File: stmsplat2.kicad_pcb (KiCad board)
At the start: 2 copper layers, 97 parts, among them J1 C11_2X36, J10 Conn_01x03_Male, J11 Conn_01x02_Male, J12 Conn_01x04_Male, J13 Conn_01x04_Male, J14 Conn_01x02, J15 Conn_01x02, J16 Screw_Terminal_01x03, J17 Screw_Terminal_01x02, J2 C12_2X36, J3 Conn_01x04_Male, J4 Conn_01x04_Male, J5 Conn_Coaxial, J6 Conn_01x06, J7 Conn_01x04_Male, J8 Conn_01x04_Male, J9 Conn_01x03_Male, Q1 BSS138LT1G, U1 ublox_chinese_PCB_module, U10 XCVR_E30-400M20S, U2 ESP32-C3-13, U3 SST25VF032B, U4 48L512-48LM01, U5 Opamp_Quad_MCP6024, U6 E180-ZG120A, U7 AZ1084C, U8 MCP6S93-X_UN, U9 DS2485

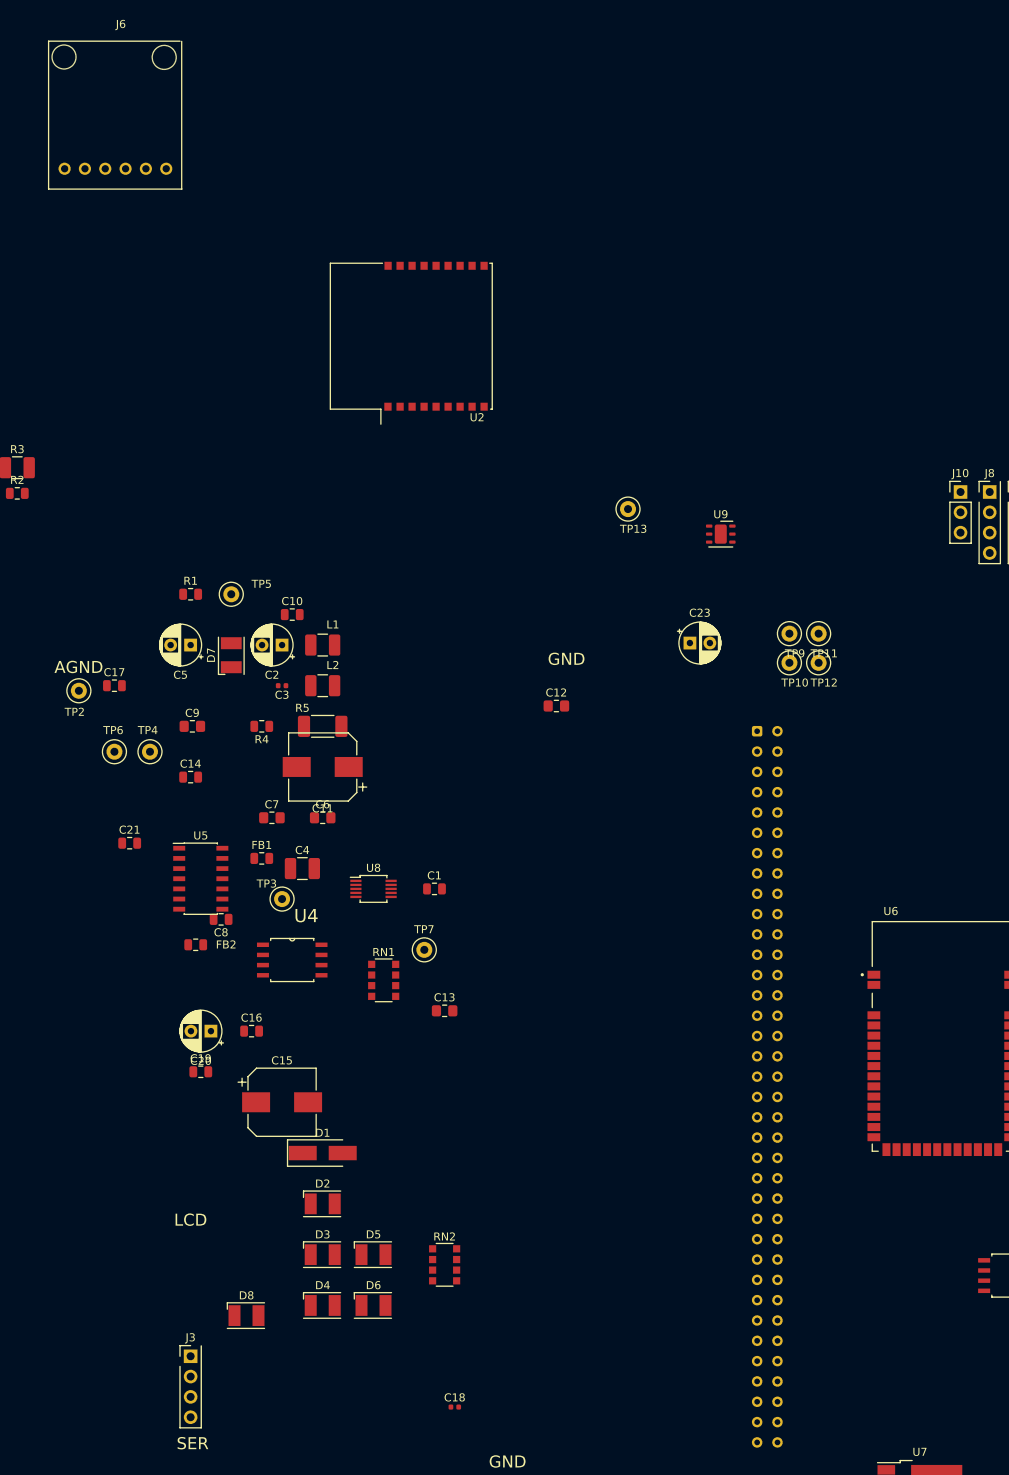
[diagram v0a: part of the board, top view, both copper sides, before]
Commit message: updated 3115 module footprint and on the PCB
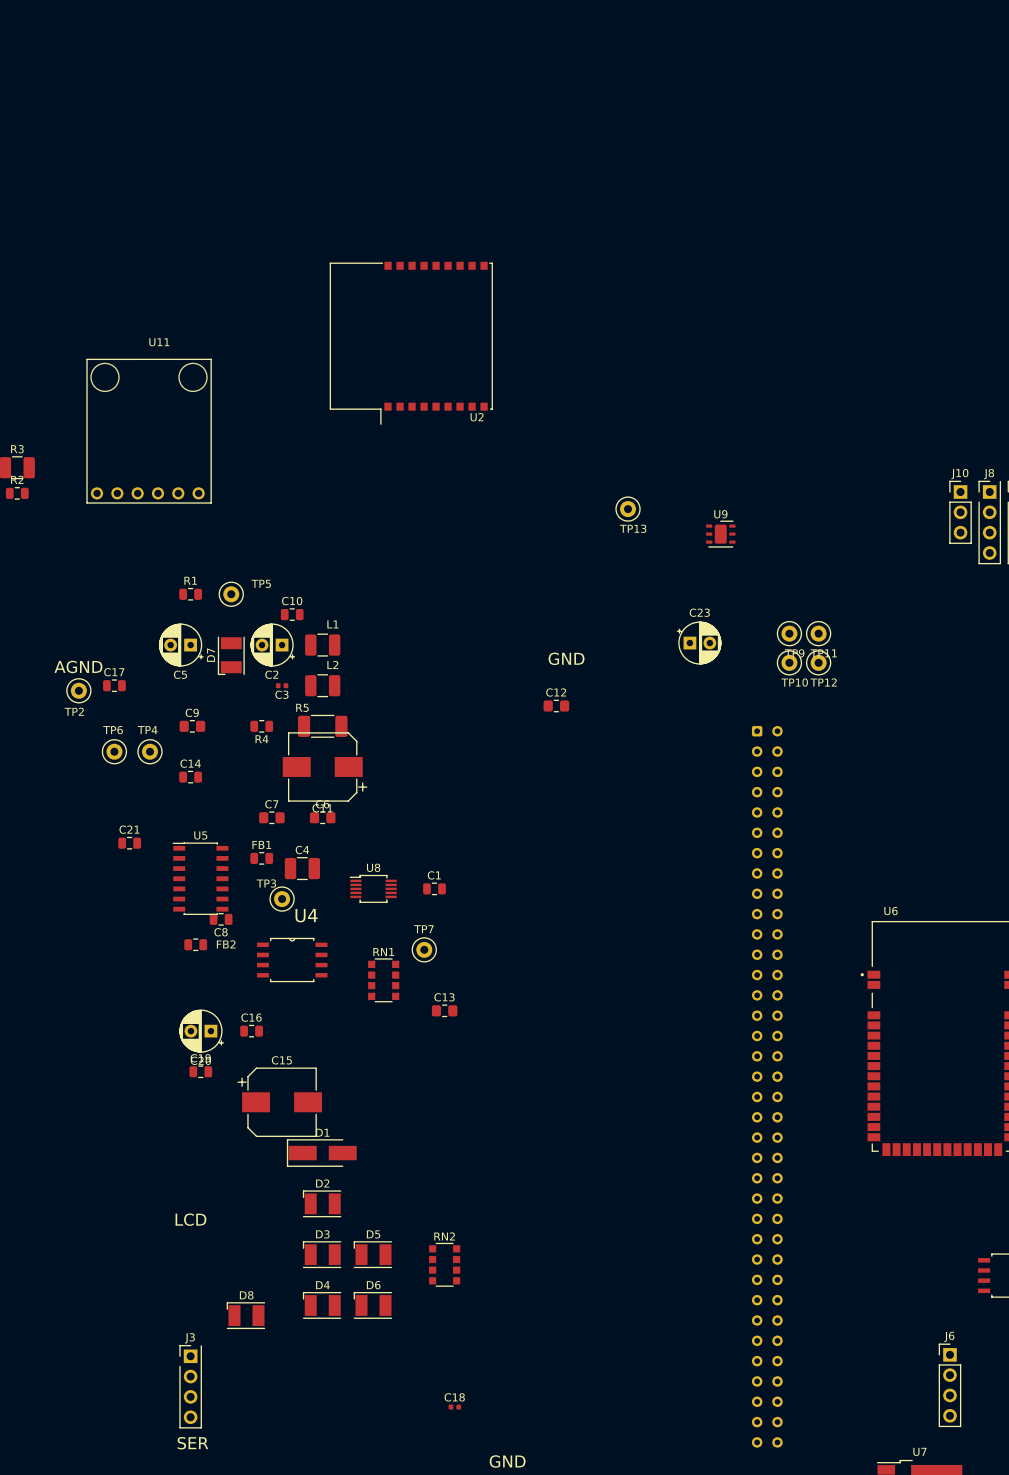
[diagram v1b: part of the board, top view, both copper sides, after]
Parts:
- added U11: 3115_module, splat2footprints:3115_PRESSURE_MODULE, F.Cu at (61.0, 7.72)
- J6: value Conn_01x06 -> Conn_01x04_Male; footprint splat2footprints:3115_PRESSURE_MODULE -> PinHeader_1x04_P2.54mm_Vertical
- U2: value ESP32-C3-13 -> ESP-C3-13U
- moved J6 198.8 mm to (168.6, 131.9)
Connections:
- net /A3V3 renamed A3V3
- net /AGND renamed GNDA
- net /NC renamed NC
- net /PA3 renamed PA3
- net /PA4 renamed PA4
- net /PB1 renamed PB1
- net /PB12 renamed PB12
- net /PB15 renamed PB15
- net /PB2 renamed PB2
- net /PB4 renamed PB4
- net /PB5 renamed PB5
- net /PB8 renamed PB8
- net /PC10 renamed PC10
- net /PC12 renamed PC12
- net /PC2 renamed PC2
- net /PC3 renamed PC3
- net /PC9 renamed PC9
- net /PD1 renamed PD1
- net /PD11 renamed PD11
- net /PD12 renamed PD12
- net /PD13 renamed PD13
- net /PD14 renamed PD14
- net /PD15 renamed PD15
- net /PD3 renamed PD3
- net /PD5 renamed PD5
- net /PD6 renamed PD6
- net /PE0 renamed PE0
- net /PE1 renamed PE1
- net /PE10 renamed PE10
- net /PE11 renamed PE11
- net /PE12 renamed PE12
- net /PE14 renamed PE14
- net /PE15 renamed PE15
- net /PE2 renamed PE2
- net /PE3 renamed PE3
- net /PE5 renamed PE5
- net /PE6 renamed PE6
- net /PE7 renamed PE7
- net /PE8 renamed PE8
- net /PF0 renamed PF0
- net /PF1 renamed PF1
- net /PF11 renamed PF11
- net /PF12 renamed PF12
- net /PF13 renamed PF13
- net /PF2 renamed PF2
- net /PF7 renamed PF7
- net /PF9 renamed PF9
- net /PG0 renamed PG0
- net /PG1 renamed PG1
- net /PG10 renamed PG10
- net /PG12 renamed PG12
- net /PG15 renamed PG15
- net /PG2 renamed PG2
- net /PG3 renamed PG3
- net /PG4 renamed PG4
- net /PG5 renamed PG5
- net /PG8 renamed PG8
- net /XB_PIO4 renamed Net-(RN1-Pad7)
- net Net-(C24-Pad2) renamed /RAWGND
- net Net-(C9-Pad1) renamed /RAW5V
- C1 pad 1: /VDD -> VDD
- C10 pad 1: /E5V -> +5V
- C11 pad 1: /+5V -> +5V
- C13 pad 1: /VDD -> VDD
- C14 pad 2: /VDD -> VDD
- C15 pad 1: /VDD -> VDD
- C16 pad 2: /VDD -> VDD
- C17 pad 2: /VDD -> VDD
- C18 pad 1: /VDD -> VDD
- C19 pad 2: /VDD -> VDD
- C2 pad 1: /VDD -> VDD
- C20 pad 1: /VDD -> VDD
- C21 pad 2: /VDD -> VDD
- C24 pad 1: /VDD -> VDD
- C3 pad 1: /VDD -> VDD
- FB1 pad 2: /E5V -> +5V
- FB2 pad 1: /VDD -> VDD
- J1 pad 18: /+5V -> +5V
- J1 pad 2: /PC11 -> PC11
- J1 pad 28: /PA0 -> PA0
- J1 pad 48: /PE4 -> PE13
- J1 pad 5: /VDD -> VDD
- J1 pad 6: /E5V -> +5V
- J1 pad 63: /PG9 -> PG9
- J12 pad 1: /VDD -> VDD
- J13 pad 1: /VDD -> VDD
- J16 pad 2: /VDD -> VDD
- J2 pad 11: /PA5 -> PA5
- J2 pad 17: /PB6 -> PB6
- J2 pad 2: /PC8 -> PC8
- J2 pad 25: /PB10 -> PA5
- J2 pad 4: /PC6 -> PC6
- J2 pad 5: /PB9 -> PB9
- J2 pad 55: /PE13 -> PE13
- J2 pad 61: /PG14 -> PE13
- J3 pad 1: /+5V -> +5V
- J4 pad 1: /VDD -> VDD
- J6 pad 1: /PB9 -> PC11
- J6 pad 2: /PC8 -> PA0
- J6 pad 3: /PB9 -> PG9
- J6 pad 4: /PB6 -> PC6
- J7 pad 1: /VDD -> VDD
- J8 pad 1: /+5V -> +5V
- Q1 pad 3: /VDD -> VDD
- R1 pad 1: /VDD -> VDD
- R1 pad 2: /PA5 -> PA5
- R11 pad 1: /VDD -> VDD
- R13 pad 1: /VDD -> VDD
- R14 pad 1: /VDD -> VDD
- R4 pad 1: /VDD -> VDD
- RN1 pad 5: /VDD -> VDD
- RN1 pad 6: /VDD -> VDD
- U1 pad 1: /VDD -> VDD
- U1 pad 5: /PA5 -> PA5
- U10 pad 19: /PE13 -> PE13
- U10 pad 9: /VDD -> VDD
- U2 pad 1: /VDD -> VDD
- U2 pad 10: /PE13 -> PE13
- U2 pad 11: /PC6 -> PC6
- U2 pad 12: /PG9 -> PG9
- U3 pad 8: /VDD -> VDD
- U4 pad 8: /VDD -> VDD
- U6 pad 11: /PC11 -> PC11
- U6 pad 12: /PA0 -> PA0
- U6 pad 13: /PC11 -> PC11
- U6 pad 3: /VDD -> VDD
- U7 pad 2: /VDD -> VDD
- U7 pad 3: /+5V -> +5V
- U9 pad 4: /PB6 -> PB6
- U9 pad 5: /PB9 -> PB9
- U9 pad 6: /VDD -> VDD

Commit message: Thrown down the components and made a 100x100 outline to see how well it might fit
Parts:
- removed RN1, RN2: 470R, Resistor_SMD:R_Array_Convex_4x1206
- added R15: 470R, Resistor_SMD:R_0805_2012Metric, F.Cu at (95.6, 156.7)
- added R16: 470R, Resistor_SMD:R_0805_2012Metric, F.Cu at (122.9, 138.1)
- added R17: 470R, Resistor_SMD:R_0805_2012Metric, F.Cu at (123.9, 131.8)
- added R18: 470R, Resistor_SMD:R_0805_2012Metric, F.Cu at (108.2, 157.0)
- added R19: 470R, Resistor_SMD:R_0805_2012Metric, F.Cu at (103.9, 157.0)
- added R20: 470R, Resistor_SMD:R_0805_2012Metric, F.Cu at (99.7, 156.8)
- added REF**: ST_Morpho_Connector_144_STLink_MountingHoles, Module:ST_Morpho_Connector_144_STLink_MountingHoles, F.Cu at (-77.9, 107.9)
- moved U2 151.2 mm to (74.7, 152.9), turned to 180 degrees
- moved C22 143.0 mm to (96.4, 137.7)
- moved J4 142.9 mm to (87.6, 135.4)
- moved J10 126.3 mm to (67.8, 98.5)
- moved TP2 126.1 mm to (111.5, 163.8)
- moved R9 125.0 mm to (77.5, 106.3)
- moved J12 122.0 mm to (124.9, 90.2)
- moved D7 121.7 mm to (105.9, 163.0), turned to 0 degrees
- moved J15 121.5 mm to (87.7, 148.7)
- moved C17 121.0 mm to (128.6, 150.6)
- moved D9 119.4 mm to (129.4, 138.4)
- moved R8 118.6 mm to (81.8, 98.9)
- moved R10 117.4 mm to (78.1, 91.2)
- moved U9 116.9 mm to (145.5, 146.1)
- moved D10 116.9 mm to (130.5, 132.4)
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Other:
- board outline added: 100 x 100 mm
- board text added: "THROWDOWN TO SEE IF IT WILL FIT"

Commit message: Ver 0.9. Initial PCB placement attempt. Some footprints changed
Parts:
- U1: footprint NEO7_GPS_MODULE -> splat2footprints:NEO7_GPS_MODULE
- moved D7 99.0 mm to (76.2, 68.6), turned to 270 degrees
- moved D6 96.3 mm to (81.3, 68.6), turned to 270 degrees
- moved D5 94.9 mm to (86.4, 68.6), turned to 270 degrees
- moved D4 94.7 mm to (91.4, 68.6), turned to 270 degrees
- moved D9 92.6 mm to (68.6, 68.6), turned to 270 degrees
- moved J16 92.0 mm to (97.4, 72.0)
- moved R18 90.9 mm to (71.9, 73.7), turned to 270 degrees
- moved FB4 90.3 mm to (90.5, 73.7)
- moved R19 87.8 mm to (76.4, 73.7), turned to 270 degrees
- moved R20 85.3 mm to (80.6, 73.7), turned to 270 degrees
- moved R16 84.2 mm to (68.6, 73.7), turned to 90 degrees
- moved R15 83.7 mm to (84.7, 73.7), turned to 270 degrees
- moved C13 82.6 mm to (68.6, 81.3)
- moved C9 78.8 mm to (96.5, 81.3), turned to 180 degrees
- moved C17 77.2 mm to (63.0, 110.0)
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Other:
- outline, holes or cut-outs redrawn
- board text added: "PLACEMENT CANDIDATE 1"
- board text added: "SPLAT2 Rev 1.0"
- board text removed: "THROWDOWN TO SEE IF IT WILL FIT"

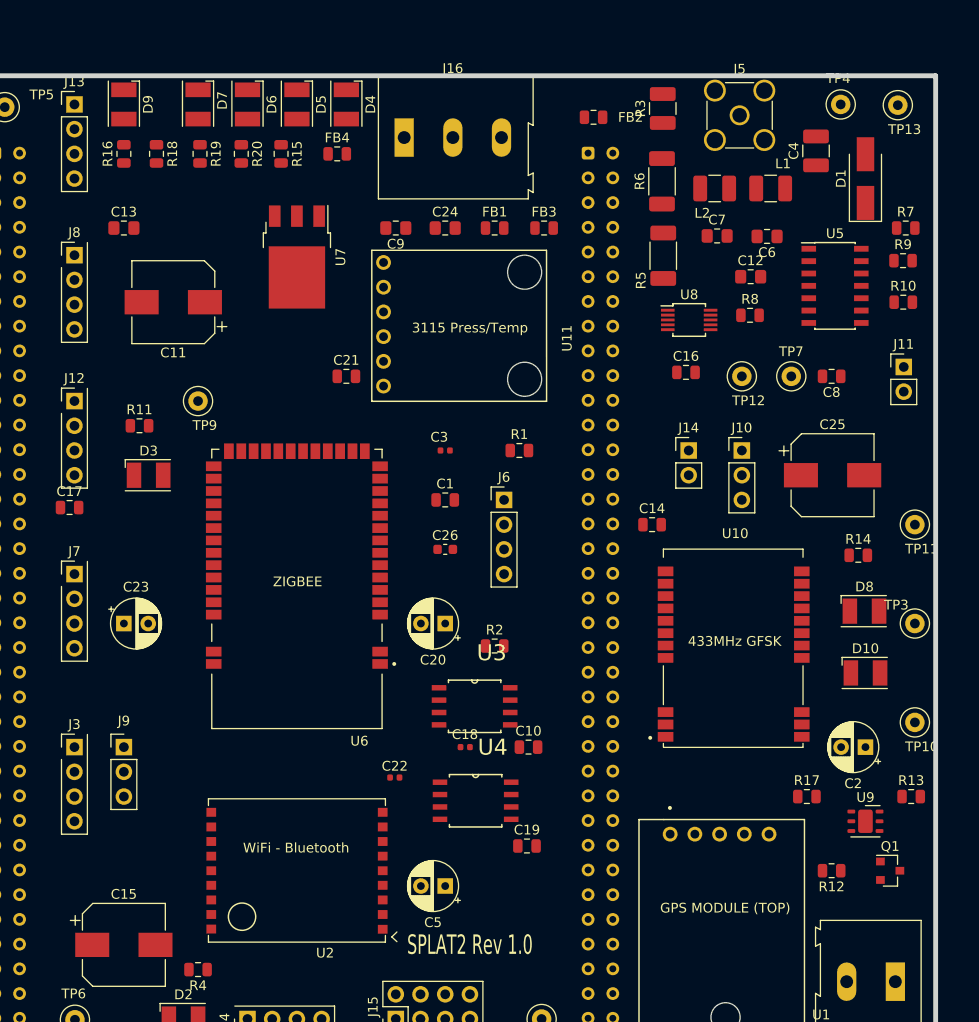
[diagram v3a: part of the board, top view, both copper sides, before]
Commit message: improved placement]
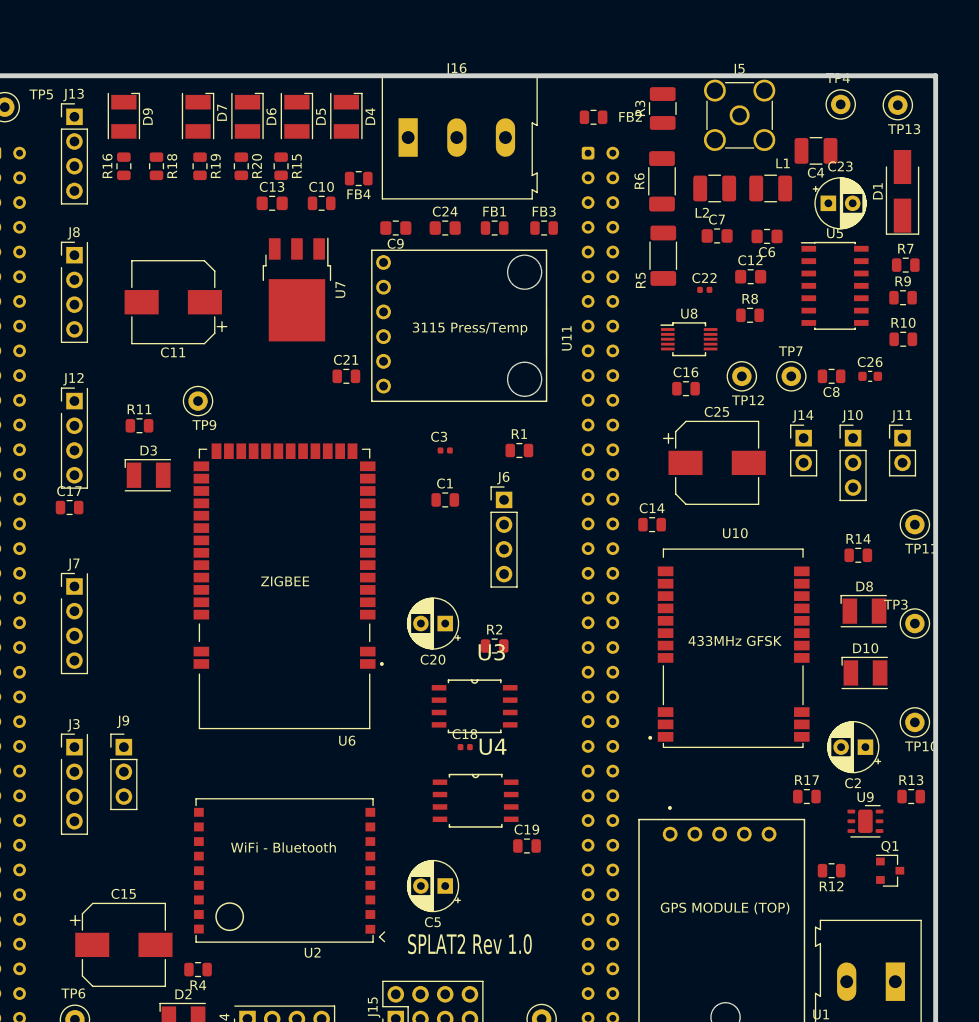
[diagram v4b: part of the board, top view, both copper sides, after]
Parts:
- moved C23 84.3 mm to (141.0, 78.7)
- moved C10 59.8 mm to (88.9, 78.7)
- moved C22 59.4 mm to (128.3, 87.6)
- moved C26 47.1 mm to (145.3, 96.5)
- moved C13 15.5 mm to (83.8, 78.7)
- moved C25 11.9 mm to (129.5, 105.4)
- moved J14 11.9 mm to (138.4, 102.9)
- moved J10 11.5 mm to (143.5, 102.9)
- moved J11 7.32 mm to (148.6, 102.9)
- moved D1 4.03 mm to (148.6, 77.5)
- moved R7 3.81 mm to (148.9, 85.1)
- moved R9 3.81 mm to (148.6, 88.4)
- moved R10 3.81 mm to (148.7, 92.7)
- moved U7 3.37 mm to (86.4, 87.6)
- moved FB4 3.37 mm to (92.7, 76.2), turned to 180 degrees
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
